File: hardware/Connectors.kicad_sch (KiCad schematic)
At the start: 9 parts, among them J1 USB_C_Receptacle_USB2.0, J14 Conn_01x05, J16 Harw_Conn_2x13, J2 Harw_Conn_1x2, J3 Harw_Conn_1x2, J8 Harw_Conn_1x4

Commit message: pcb update
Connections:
- net AIR_M: now also J16.3
- net AIR_P: now also J16.7
- net AIR_PRE: now also J16.10
- net AMS_SAFETY_1: now also J16.25; no longer J16.26
- net AMS_SAFETY_2: now also J16.24; no longer J16.25
- net at F1.2: now also J16.26; no longer J16.2
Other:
- moved on the sheet: F1
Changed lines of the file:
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@@
     (stroke (width 0) (type default) (color 0 0 0 0))
   )
-  (wire (pts (xy 84.455 127) (xy 81.915 127))
+  (wire (pts (xy 84.455 124.46) (xy 81.915 124.46))
     (stroke (width 0) (type default) (color 0 0 0 0))
   )
@@
     (stroke (width 1) (type default) (color 132 0 0 1))
   )
-  (wire (pts (xy 62.865 99.06) (xy 61.595 99.06))
+  (wire (pts (xy 88.265 127) (xy 89.535 127))
     (stroke (width 0) (type default) (color 0 0 0 0))
   )
@@
     (stroke (width 0) (type default) (color 0 0 0 0))
   )
-  (wire (pts (xy 34.29 111.76) (xy 31.75 111.76))
+  (wire (pts (xy 69.215 101.6) (xy 66.675 101.6))
     (stroke (width 0) (type default) (color 0 0 0 0))
   )
@@
     (stroke (width 0) (type default) (color 0 0 0 0))
   )
-  (wire (pts (xy 34.29 109.22) (xy 31.75 109.22))
+  (wire (pts (xy 69.215 119.38) (xy 66.675 119.38))
     (stroke (width 0) (type default) (color 0 0 0 0))
   )
@@
     (stroke (width 0) (type default) (color 0 0 0 0))
   )
-  (wire (pts (xy 69.215 99.06) (xy 67.945 99.06))
+  (wire (pts (xy 81.915 127) (xy 83.185 127))
     (stroke (width 0) (type default) (color 0 0 0 0))
   )
@@
     (stroke (width 0) (type default) (color 0 0 0 0))
   )
-  (wire (pts (xy 112.395 111.76) (xy 114.935 111.76))
+  (wire (pts (xy 69.215 111.76) (xy 66.675 111.76))
     (stroke (width 0) (type default) (color 0 0 0 0))
   )
@@
     (stroke (width 0) (type default) (color 0 0 0 0))
   )
-  (wire (pts (xy 81.915 124.46) (xy 84.455 124.46))
+  (wire (pts (xy 81.915 121.92) (xy 84.455 121.92))
     (stroke (width 0) (type default) (color 0 0 0 0))
   )
@@
     )
   )
-  (global_label "AIR_PRE" (shape input) (at 31.75 109.22 180) (fields_autoplaced)
-    (effects (font (size 1.27 1.27)) (justify right))
-    (property "Intersheet References" "${INTERSHEET_REFS}" (id 0) (at 21.8058 109.2994 0)
+  (global_label "AIR_PRE" (shape input) (at 66.675 119.38 180) (fields_autoplaced)
+    (effects (font (size 1.27 1.27)) (justify right))
+    (property "Intersheet References" "${INTERSHEET_REFS}" (id 0) (at 56.7308 119.4594 0)
       (effects (font (size 1.27 1.27)) (justify right) hide)
     )
@@
     )
   )
-  (global_label "AMS_SAFETY_2" (shape input) (at 84.455 124.46 0) (fields_autoplaced)
+  (global_label "AMS_SAFETY_2" (shape input) (at 84.455 121.92 0) (fields_autoplaced)
+    (effects (font (size 1.27 1.27)) (justify left))
+    (property "Intersheet References" "${INTERSHEET_REFS}" (id 0) (at 100.2654 121.9994 0)
+      (effects (font (size 1.27 1.27)) (justify left) hide)
+    )
+  )
+  (global_label "SWDIO" (shape input) (at 178.435 142.24 180) (fields_autoplaced)
+    (effects (font (size 1.27 1.27)) (justify right))
+    (property "Intersheet References" "${INTERSHEET_REFS}" (id 0) (at 170.2446 142.1606 0)
+      (effects (font (size 1.27 1.27)) (justify right) hide)
+    )
+  )
+  (global_label "AIR_M" (shape input) (at 66.675 101.6 180) (fields_autoplaced)
+    (effects (font (size 1.27 1.27)) (justify right))
+    (property "Intersheet References" "${INTERSHEET_REFS}" (id 0) (at 58.9684 101.6794 0)
+      (effects (font (size 1.27 1.27)) (justify right) hide)
+    )
+  )
+  (global_label "AMS_SAFETY_1" (shape input) (at 84.455 124.46 0) (fields_autoplaced)
     (effects (font (size 1.27 1.27)) (justify left))
     (property "Intersheet References" "${INTERSHEET_REFS}" (id 0) (at 100.2654 124.5394 0)
@@
     )
   )
-  (global_label "SWDIO" (shape input) (at 178.435 142.24 180) (fields_autoplaced)
-    (effects (font (size 1.27 1.27)) (justify right))
-    (property "Intersheet References" "${INTERSHEET_REFS}" (id 0) (at 170.2446 142.1606 0)
-      (effects (font (size 1.27 1.27)) (justify right) hide)
-    )
-  )
-  (global_label "AIR_M" (shape input) (at 31.75 111.76 180) (fields_autoplaced)
-    (effects (font (size 1.27 1.27)) (justify right))
-    (property "Intersheet References" "${INTERSHEET_REFS}" (id 0) (at 24.0434 111.8394 0)
-      (effects (font (size 1.27 1.27)) (justify right) hide)
-    )
-  )
-  (global_label "AMS_SAFETY_1" (shape input) (at 84.455 127 0) (fields_autoplaced)
-    (effects (font (size 1.27 1.27)) (justify left))
-    (property "Intersheet References" "${INTERSHEET_REFS}" (id 0) (at 100.2654 127.0794 0)
-      (effects (font (size 1.27 1.27)) (justify left) hide)
-    )
-  )
   (global_label "D+" (shape input) (at 253.365 114.3 0) (fields_autoplaced)
     (effects (font (size 1.27 1.27)) (justify left))
@@
     )
   )
-  (global_label "AIR_P" (shape input) (at 114.935 111.76 0) (fields_autoplaced)
-    (effects (font (size 1.27 1.27)) (justify left))
-    (property "Intersheet References" "${INTERSHEET_REFS}" (id 0) (at 122.4602 111.6806 0)
-      (effects (font (size 1.27 1.27)) (justify left) hide)
+  (global_label "AIR_P" (shape input) (at 66.675 111.76 180) (fields_autoplaced)
+    (effects (font (size 1.27 1.27)) (justify right))
+    (property "Intersheet References" "${INTERSHEET_REFS}" (id 0) (at 59.1498 111.8394 0)
+      (effects (font (size 1.27 1.27)) (justify right) hide)
     )
   )
@@
     )
   )
-  (symbol (lib_id "Device:Fuse_Small") (at 65.405 99.06 0) (unit 1)
-    (in_bom yes) (on_board yes)
-    (property "Reference" "F1" (id 0) (at 50.165 98.425 0)
+  (symbol (lib_id "Device:Fuse_Small") (at 85.725 127 180) (unit 1)
+    (in_bom yes) (on_board yes)
+    (property "Reference" "F1" (id 0) (at 104.14 127.635 0)
       (effects (font (size 1.27 1.27)) (justify left))
     )
-    (property "Value" "0.5A" (id 1) (at 49.53 100.33 0)
+    (property "Value" "0.5A" (id 1) (at 104.775 125.73 0)
       (effects (font (size 1.27 1.27)) (justify left))
     )
-    (property "Footprint" "Fuse:Fuse_1206_3216Metric" (id 2) (at 65.405 99.06 0)
-      (effects (font (size 1.27 1.27)) hide)
-    )
-    (property "Datasheet" "~" (id 3) (at 65.405 99.06 0)
+    (property "Footprint" "Fuse:Fuse_1206_3216Metric" (id 2) (at 85.725 127 0)
+      (effects (font (size 1.27 1.27)) hide)
+    )
+    (property "Datasheet" "~" (id 3) (at 85.725 127 0)
       (effects (font (size 1.27 1.27)) hide)
     )
@@
     (pin "1")
   )
-  (symbol (lib_id "power:+5V") (at 61.595 99.06 90) (unit 1)
-    (in_bom yes) (on_board yes)
-    (property "Reference" "#PWR03" (id 0) (at 65.405 99.06 0)
-      (effects (font (size 1.27 1.27)) hide)
-    )
-    (property "Value" "+5V" (id 1) (at 56.515 99.06 90))
-    (property "Footprint" "" (id 2) (at 61.595 99.06 0)
-      (effects (font (size 1.27 1.27)) hide)
-    )
-    (property "Datasheet" "" (id 3) (at 61.595 99.06 0)
-      (effects (font (size 1.27 1.27)) hide)
-    )
+  (symbol (lib_id "power:+5V") (at 89.535 127 270) (unit 1)
+    (in_bom yes) (on_board yes)
+    (property "Reference" "#PWR03" (id 0) (at 85.725 127 0)
+      (effects (font (size 1.27 1.27)) hide)
+    )
+    (property "Value" "+5V" (id 1) (at 94.615 127 90))
+    (property "Footprint" "" (id 2) (at 89.535 127 0)
+      (effects (font (size 1.27 1.27)) hide)
+    )
+    (property "Datasheet" "" (id 3) (at 89.535 127 0)
+      (effects (font (size 1.27 1.27)) hide)
+    )

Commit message: schemat sync
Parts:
- removed J16: Harw_Conn_2x13, M80-85126YY, symbol Harwin 26 pin 90 deg:Harw_Conn_2x13
- removed J2: Harw_Conn_1x2, M808420245, symbol Harwin 2 pin 90 deg:Harw_Conn_1x2
- removed J3: Harw_Conn_1x2, Harwin 2 pin 90 deg:M808420245, symbol Harwin 2 pin 90 deg:Harw_Conn_1x2
- removed J8: Harw_Conn_1x4, M80-8420445, symbol Harwin 4 pin 90 deg:Harw_Conn_1x4
- added J2: Harw_Conn_2x13, M80-85126YY, symbol Harwin 26 pin 90 deg:Harw_Conn_2x13
- added J3: M300-MV31045M1, M300MV31045M1, symbol M300-MV31045M1:M300-MV31045M1
- added J4, J5: Harw_Conn_1x2, M808420245, symbol Harwin 2 pin 90 deg:Harw_Conn_1x2
- added J6: Harw_Conn_1x4, M80-8420445, symbol Harwin 4 pin 90 deg:Harw_Conn_1x4
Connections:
- net AMS_FAULT_COCKPIT: now also J2.13
- net AMS_SAFETY_1: now also J2.25
- net AMS_SAFETY_2: now also J2.24
- net D+: now also J6.2
- net D-: now also J6.3
- net GND: now also J2.14, J2.15, J2.MH, J3.1, J3.2, J3.3
- net HV_ACU+: now also J5.2
- net HV_ACU-: now also J5.1
- net HV_CAR+: now also J4.2
- net HV_CAR-: now also J4.1
- net ISO_GND: now also J4.MH, J5.MH
- net USB_GND: now also J6.1, J6.MH
- net VBUS: now also J6.4
- net VDD: now also J2.1
- net at F1.2: now also J2.26
- new net AIR_M+: J3.10, J3.4, J3.6, J3.8
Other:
- moved on the sheet: F1

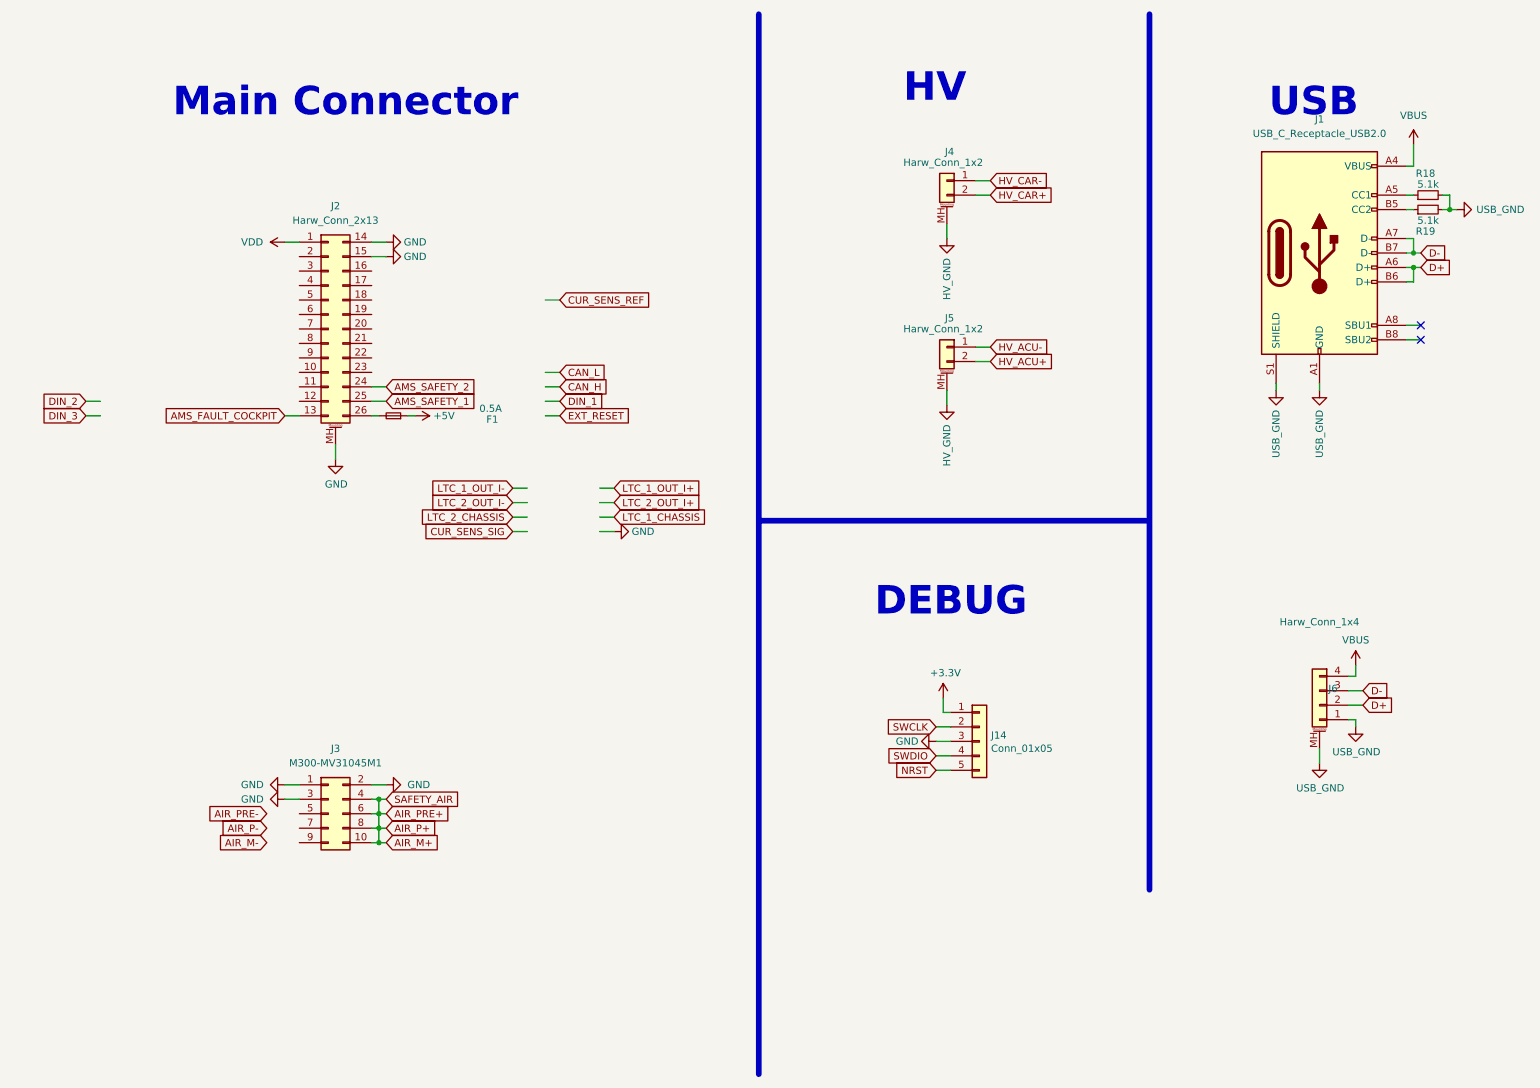
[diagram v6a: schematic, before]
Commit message: measurments section changes, sorted components on the board into groups, changed main connector and added seprate for AIRs, added IMD PWM input as well as AIR fault detection
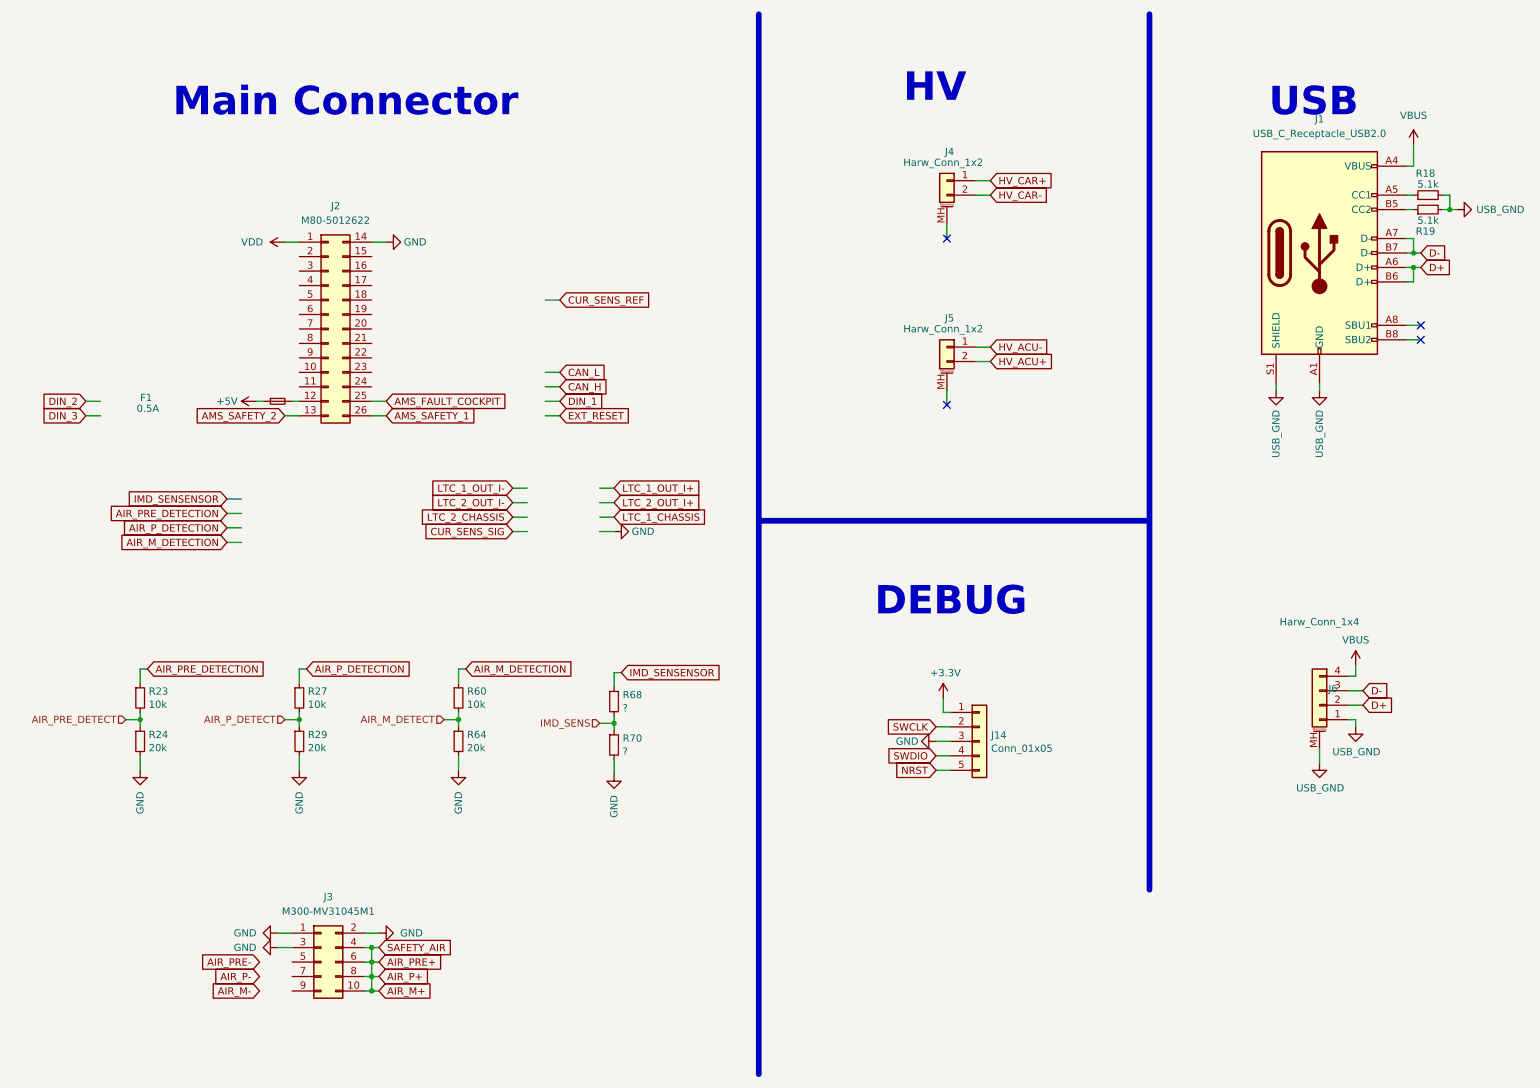
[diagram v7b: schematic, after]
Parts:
- removed J2: Harw_Conn_2x13, M80-85126YY, symbol Harwin 26 pin 90 deg:Harw_Conn_2x13
- added J2: M80-5012622, M80-50126YY, symbol M80-5012622:M80-5012622
- added R23, R27, R60: 10k, Resistor_SMD:R_0603_1608Metric, symbol Device:R_Small
- added R24, R29, R64: 20k, Resistor_SMD:R_0603_1608Metric, symbol Device:R_Small
- added R68, R70: ?, Resistor_SMD:R_0603_1608Metric, symbol Device:R_Small
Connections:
- net AMS_FAULT_COCKPIT: now also J2.25
- net AMS_SAFETY_1: now also J2.26
- net AMS_SAFETY_2: now also J2.13
- net GND: now also J2.14, R24.2, R29.2, R64.2, R70.2
- net HV_CAR+: now also J4.1; no longer J4.2
- net HV_CAR-: now also J4.2; no longer J4.1
- net VDD: now also J2.1
- net at F1.2: now also J2.12
- net ISO_GND: no longer names the net of J4.MH
- net ISO_GND: no longer J5.MH
- new net AIR_M_DETECT: R60.2, R64.1
- new net AIR_M_DETECTION: R60.1
- new net AIR_PRE_DETECT: R23.2, R24.1
- new net AIR_PRE_DETECTION: R23.1
- new net AIR_P_DETECT: R27.2, R29.1
- new net AIR_P_DETECTION: R27.1
- new net IMD_SENS: R68.2, R70.1
- new net IMD_SENSENSOR: R68.1
- no-connect marks 2 -> 4
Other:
- moved on the sheet: F1, J3

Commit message: changed few connectors, finished board HV section and other minor changes
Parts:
- removed J2: M80-5012622, M80-50126YY, symbol M80-5012622:M80-5012622
- removed J4, J5: Harw_Conn_1x2, M808420245, symbol Harwin 2 pin 90 deg:Harw_Conn_1x2
- removed J6: Harw_Conn_1x4, M80-8420445, symbol Harwin 4 pin 90 deg:Harw_Conn_1x4
- added J2: M80-5302642, M80-53026YY, symbol M80-5302642:M80-5302642
- added J4, J5, J6: M80-5L10442MC, M80-5L104YYMC, symbol M80-5L10442MC:M80-5L10442MC
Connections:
- net AIR_M+: no longer J3.10, J3.4, J3.6, J3.8
- net AMS_FAULT_COCKPIT: now also J2.25
- net AMS_SAFETY_1: now also J2.13
- net AMS_SAFETY_2: now also J2.26
- net D+: now also J6.4
- net D-: now also J6.3
- net GND: now also J2.14; no longer J3.1, J3.2, J3.3
- net HV_ACU+: now also J5.3, J5.4
- net HV_ACU-: now also J5.1, J5.2
- net HV_CAR+: now also J4.3, J4.4
- net HV_CAR-: now also J4.1, J4.2
- net USB_GND: now also J6.2
- net VBUS: now also J6.1
- net VDD: now also J2.1
- net at F1.2: now also J2.12
- no-connect marks 4 -> 2
